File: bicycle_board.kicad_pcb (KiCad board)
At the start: 2 copper layers, 132 parts, among them J1 Conn_02x05_Odd_Even, J10 USB_A, J11 Conn_01x02, J12 Conn_01x04, J13 Conn_01x04, J2 USB_C_Receptacle_USB2.0_16P, J3 Conn_01x02, J4 Conn_01x02, J5 Micro_SD_Card, J6 Conn_01x08, J7 Conn_01x03, J8 Conn_01x02, J9 Conn_01x06, Q1 Q_NMOS_GSD, Q2 Q_NMOS_GSD, Q3 Q_NMOS_GSD, Q4 Q_NMOS_GSD, Q5 Q_NMOS_GSD, Q6 Si2302, Q7 Si2302, Q8 Q_PMOS_GSD, U1 TP4056, U10 MCP603-xCH, U11 BMP280, U12 MMC5633NJL, U13 NS4168, U14 ESP32-C3-WROOM-02U, U15 CH32V203C8T6, U16 PS7516, U17 TXB0108PW, U2 SGM2039, U3 IIM-42652, U4 QMI8610, U5 AHT20, U6 SGM2033-1.8, U7 74HC595, U8 74HC595, U9 PCA9306DC1, Y1 12MHz, Y2 32.768kHz

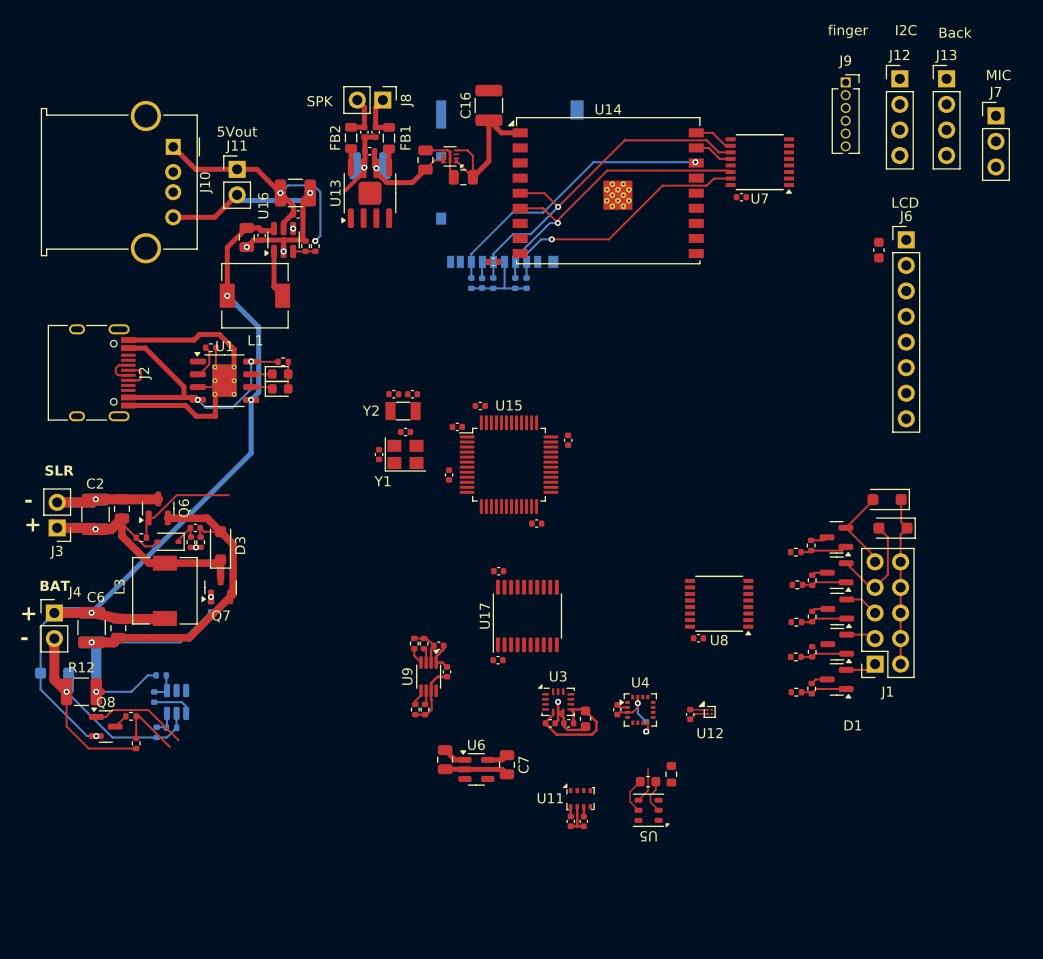
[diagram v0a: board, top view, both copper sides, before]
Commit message: 初步划定PCB边缘，改为紧凑布局
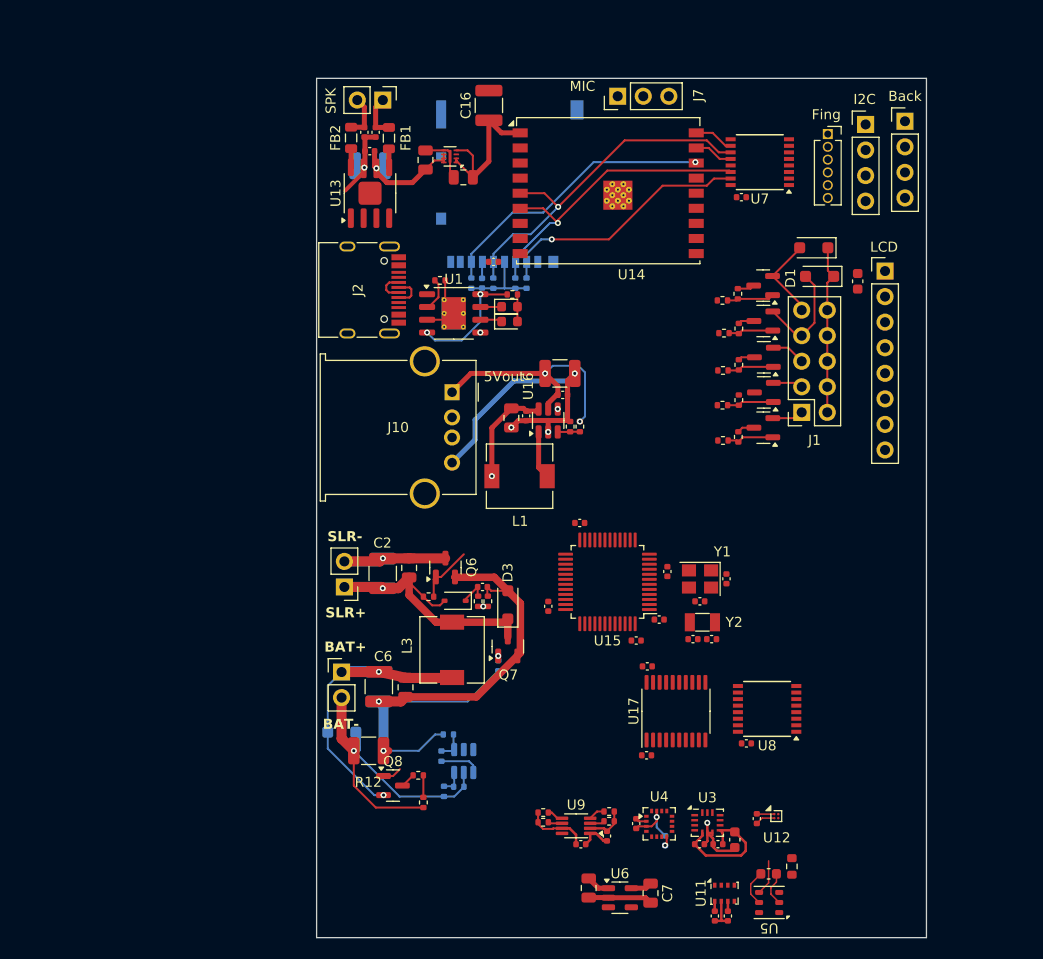
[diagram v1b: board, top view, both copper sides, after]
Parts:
- removed J11: Conn_01x02, Connector_PinHeader_2.54mm:PinHeader_1x02_P2.54mm_Vertical
- moved C23 39.9 mm to (139.8, 112.8), turned to 180 degrees
- moved J7 37.6 mm to (130.5, 58.9), turned to 90 degrees
- moved C22 37.0 mm to (138.0, 112.8), turned to 0 degrees
- moved J10 36.9 mm to (114.0, 88.3)
- moved C24 36.7 mm to (141.3, 106.8), turned to -90 degrees
- moved Y2 36.4 mm to (138.9, 111.2), turned to 180 degrees
- moved C25 33.7 mm to (138.7, 109.1), turned to 0 degrees
- moved C45 31.8 mm to (121.4, 90.6)
- moved C44 31.8 mm to (119.9, 90.8)
- moved C46 31.8 mm to (124.8, 86.4)
- moved C47 31.8 mm to (125.0, 88.6)
- moved L1 31.8 mm to (120.8, 96.6)
- moved R33 31.8 mm to (126.7, 91.7)
- moved R34 31.8 mm to (125.8, 91.7)
- moved U16 31.8 mm to (123.6, 91.1)
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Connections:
- net /power/5V_EN renamed /power/5VOUT_EN
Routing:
- net +BATT: track 94.8 -> 55.2 mm
- net GND: track 135.5 -> 113.1 mm
- net /power/VUSB: track 27.0 -> 11.8 mm
- net /batsamp_en: track 9.70 -> 1.92 mm
- net /PWM_solar: track 10.9 -> 5.76 mm
- net /ADC_Vbat: track 6.80 -> 2.18 mm
- net +5V: track 26.7 -> 24.2 mm
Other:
- board outline added: 60.6 x 85.4 mm
- board text added: "BAT+"
- board text added: "BAT-"
- board text added: "SLR+"
- board text added: "SLR-"
- board text removed: "+ -"
- board text removed: "- +"
- board text removed: "BAT"
- board text removed: "Back"
- board text removed: "I2C"
- board text removed: "LCD"
- board text removed: "SLR"
- board text removed: "SPK"
- board text removed: "finger"

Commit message: 收窄PCB宽度到47.4mm
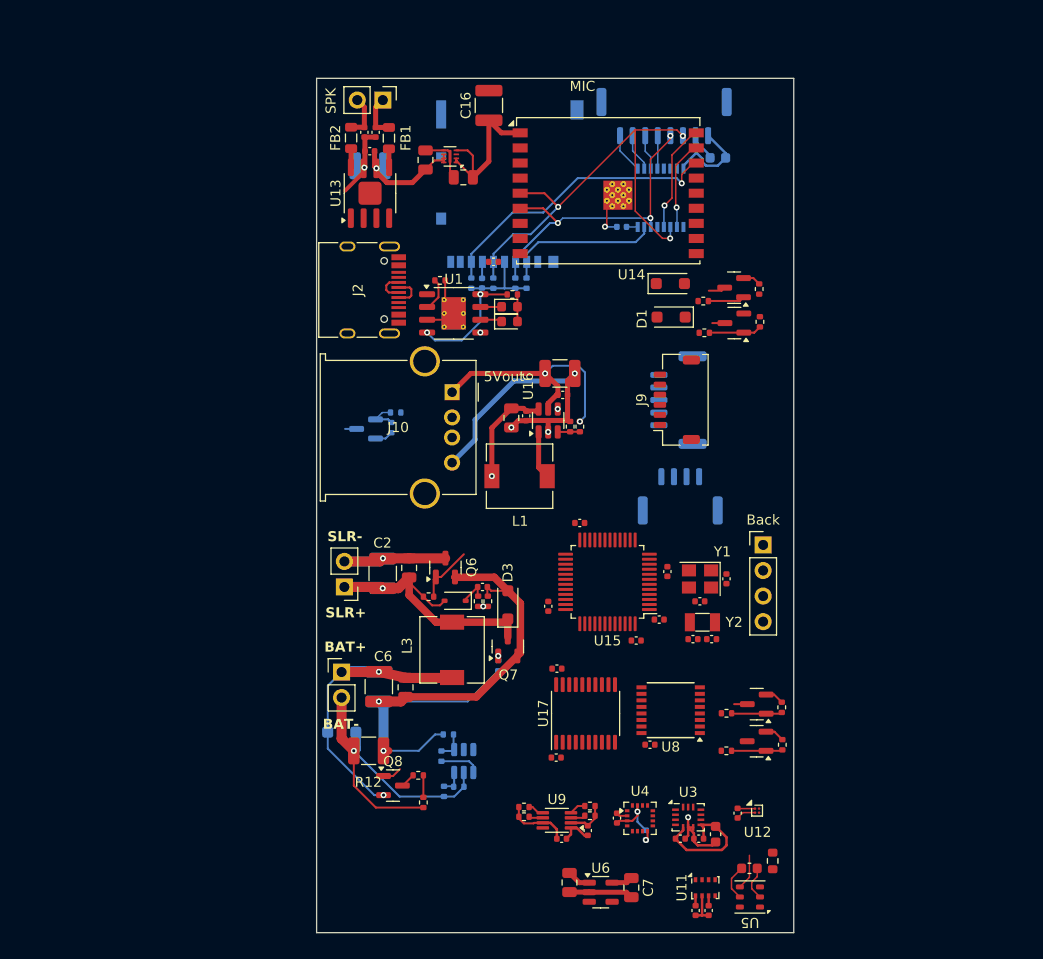
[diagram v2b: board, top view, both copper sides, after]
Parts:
- removed J1: Conn_02x05_Odd_Even, Connector_PinSocket_2.54mm:PinSocket_2x05_P2.54mm_Vertical
- C14, C42, Q1, R1, R2, U7: moved to B.Cu
- J12: footprint Connector_PinHeader_2.54mm:PinHeader_1x04_P2.54mm_Vertical -> Connector_JST:JST_GH_BM04B-GHS-TBT_1x04-1MP_P1.25mm_Vertical; moved to B.Cu
- J6: footprint Connector_PinHeader_2.54mm:PinHeader_1x08_P2.54mm_Vertical -> Connector_JST:JST_GH_BM08B-GHS-TBT_1x08-1MP_P1.25mm_Vertical; moved to B.Cu
- J7: value Conn_01x03 -> Conn_01x05; footprint Connector_PinHeader_2.54mm:PinHeader_1x03_P2.54mm_Vertical -> Connector_JST:JST_GH_BM05B-GHS-TBT_1x05-1MP_P1.25mm_Vertical; moved to B.Cu
- J9: footprint Connector_PinSocket_1.27mm:PinSocket_1x06_P1.27mm_Vertical -> Connector_JST:JST_SHL_SM06B-SHLS-TF_1x06-1MP_P1.00mm_Horizontal
- moved J13 44.4 mm to (145.0, 103.5)
- moved J12 41.3 mm to (136.7, 98.6)
- moved Q1 39.5 mm to (105.5, 91.9)
- moved Q2 34.7 mm to (144.3, 123.0)
- moved R3 34.5 mm to (146.9, 123.3)
- moved R1 34.5 mm to (108.0, 91.8), turned to -90 degrees
- moved Q3 34.5 mm to (144.3, 119.3)
- moved R7 34.3 mm to (141.3, 123.9)
- moved R4 34.3 mm to (146.8, 119.6)
- moved R8 34.1 mm to (141.3, 120.2)
- moved R2 32.6 mm to (108.4, 90.3), turned to 180 degrees
- moved J7 30.8 mm to (136.5, 89.1)
- moved J9 30.4 mm to (136.4, 89.0), turned to 90 degrees
- moved J6 26.8 mm to (135.1, 60.9), turned to 180 degrees
- moved C14 18.5 mm to (140.5, 65.0), turned to 0 degrees
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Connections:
- J7 pad 1: /I2SI_WS -> unconnected-(J7-Pin_1-Pad1)
- J7 pad 2: /I2SI_BCK -> unconnected-(J7-Pin_2-Pad2)
- J7 pad 3: /I2SI_SD -> /I2SI_WS
- Q1 pad 3: Net-(J1-Pin_1) -> unconnected-(Q1-D-Pad3)
- Q2 pad 3: Net-(J1-Pin_3) -> unconnected-(Q2-D-Pad3)
- Q3 pad 3: Net-(J1-Pin_5) -> Net-(D2-A)
- U14 pad 17: /595_RCLK -> /595_CLR
- U14 pad 18: /595_CLR -> /595_RCLK
- U7 pad 1: /SPI_CS_LCD -> /LCD_BL
- U7 pad 2: /SPI_CS_STM32 -> /SPI_CS_LCD
- U7 pad 3: /LED_WIFIBT -> /LCD_RST
- U7 pad 5: /LCD_RST -> unconnected-(U7-QF-Pad5)
- U7 pad 6: /LCD_BL -> /SPI_CS_STM32
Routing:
- net Net-(D1-K): track 16.9 -> 0.00 mm
- net GND: track 113.1 -> 125.9 mm, vias 7 -> 8
- net Net-(D1-A): track 12.3 -> 1.26 mm
- net /SPI_CS_SD: track 25.8 -> 15.6 mm, vias 1 -> 0
- net /SPI_SCLK: track 35.5 -> 44.7 mm, vias 1 -> 3
- net Net-(D2-A): track 10.2 -> 3.01 mm
- net /595_RCLK: track 3.87 -> 10.8 mm, vias 0 -> 1
- net /595_CLR: track 3.95 -> 8.93 mm, vias 0 -> 1
- net Net-(J1-Pin_1): track 4.83 -> 0.00 mm
- net /LCD_BL: track 0.00 -> 4.00 mm
- net +3.3V: track 32.5 -> 36.4 mm
- net /SPI_CS_LCD: track 0.00 -> 3.75 mm
- net /LCD_RST: track 0.00 -> 3.50 mm
- net Net-(J1-Pin_5): track 3.38 -> 0.00 mm
- net /LCD_DC: track 0.00 -> 3.29 mm
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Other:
- board size 60.6 x 85.4 mm -> 47.4 x 84.9 mm

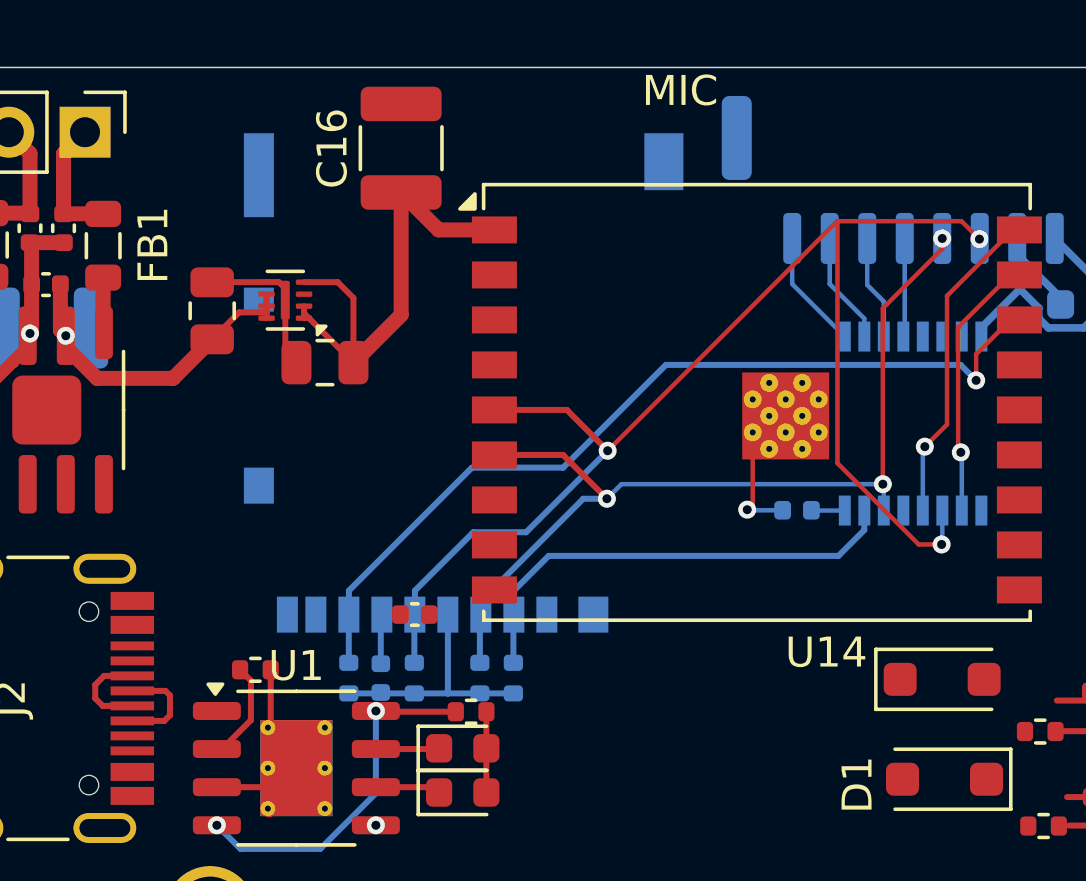
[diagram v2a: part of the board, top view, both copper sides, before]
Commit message: 画我现有的SD卡槽封装，应用到PCB
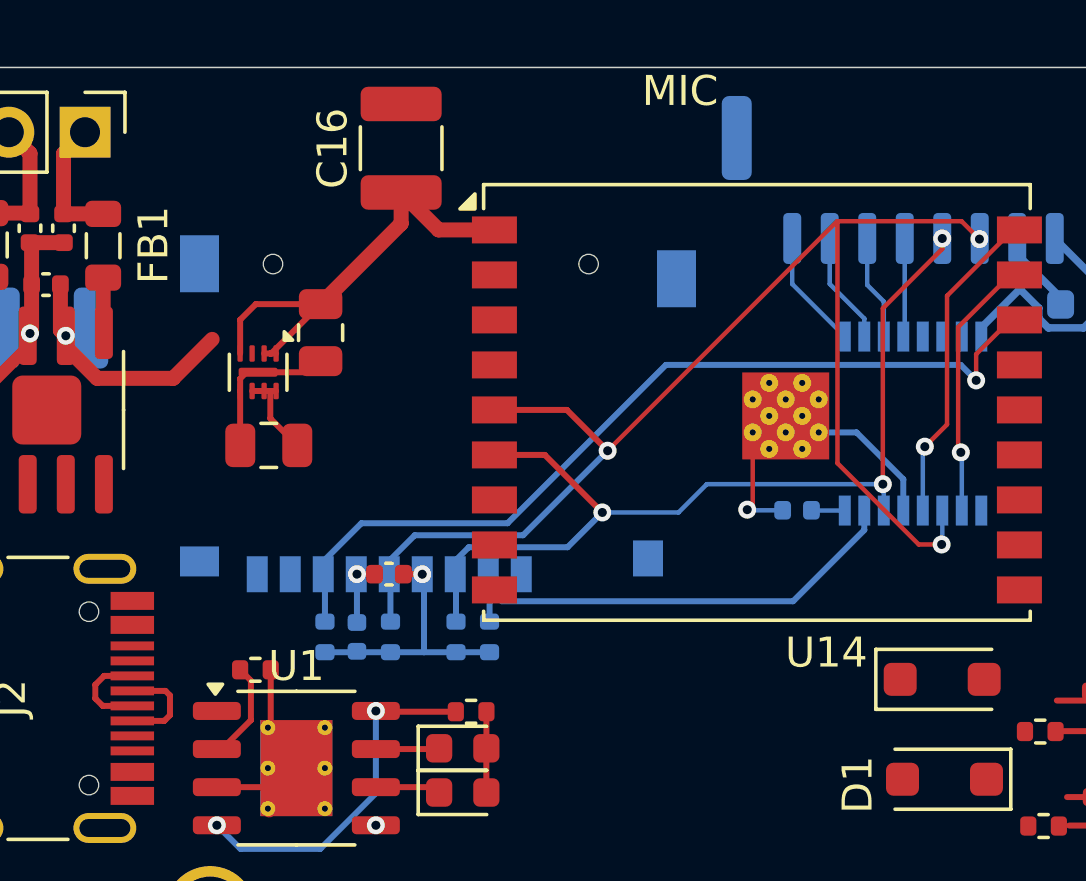
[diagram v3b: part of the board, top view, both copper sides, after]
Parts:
- removed J5: Micro_SD_Card, Connector_Card:microSD_HC_Hirose_DM3AT-SF-PEJM5
- added J1: Micro_SD_Card, Library:microSD_Slot_mybuy, B.Cu at (118.9, 66.3)
- moved C3 4.87 mm to (113.3, 69.7), turned to 180 degrees
- moved U2 2.57 mm to (112.9, 67.3), turned to -90 degrees
- moved C32 1.60 mm to (117.3, 74.0)
- moved C13 1.59 mm to (116.2, 76.1)
- moved R28 1.59 mm to (119.5, 76.1)
- moved R30 1.59 mm to (117.3, 76.1)
- moved R31 1.59 mm to (115.2, 76.1)
- moved R27 1.59 mm to (120.7, 76.1)
- moved C8 1.01 mm to (115.0, 65.9), turned to -90 degrees
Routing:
- net GND: track 125.9 -> 131.0 mm, vias 8 -> 9
- net +3.3V: track 36.4 -> 35.5 mm, vias 0 -> 1
- net /SPI_CS_SD: track 15.6 -> 16.4 mm

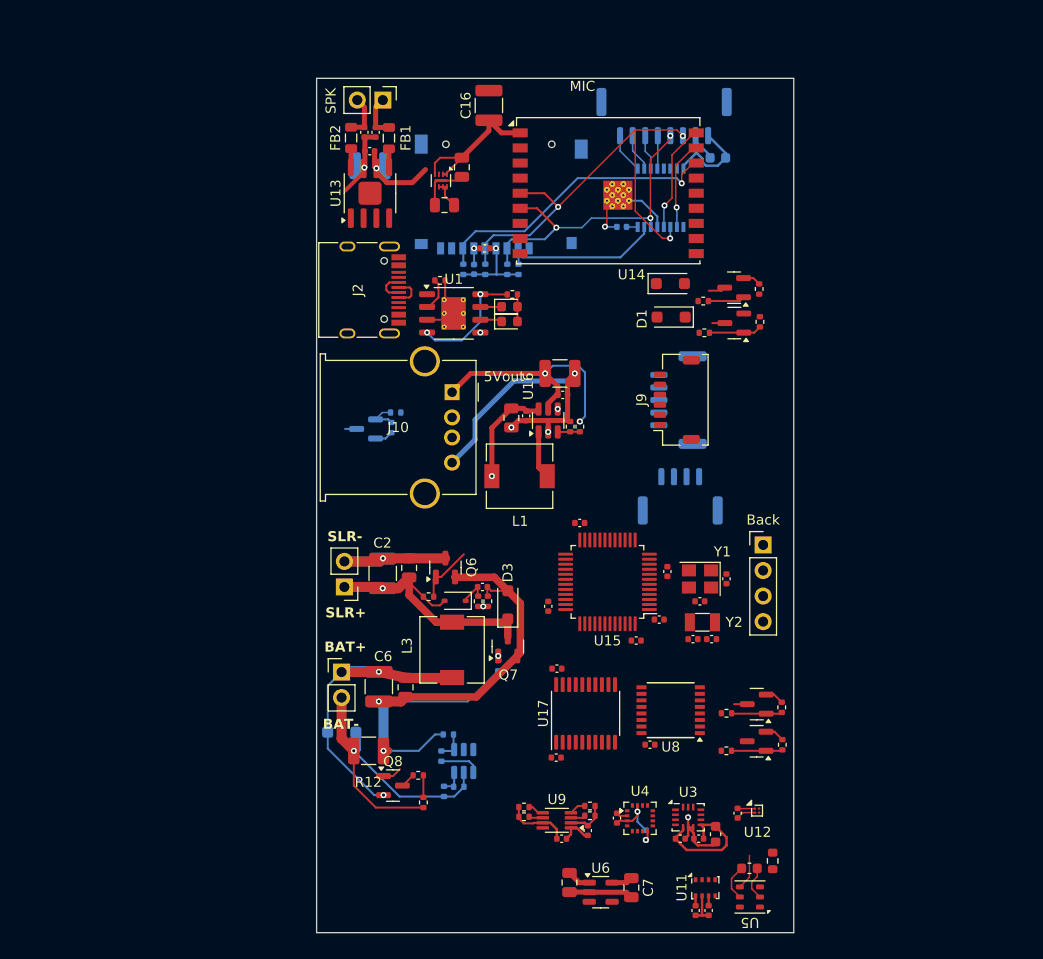
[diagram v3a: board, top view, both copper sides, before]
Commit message: PCB宽度进一步收缩到41.4mm，晶振改2016和2012，最小线距改0.15mm，添加一些布线
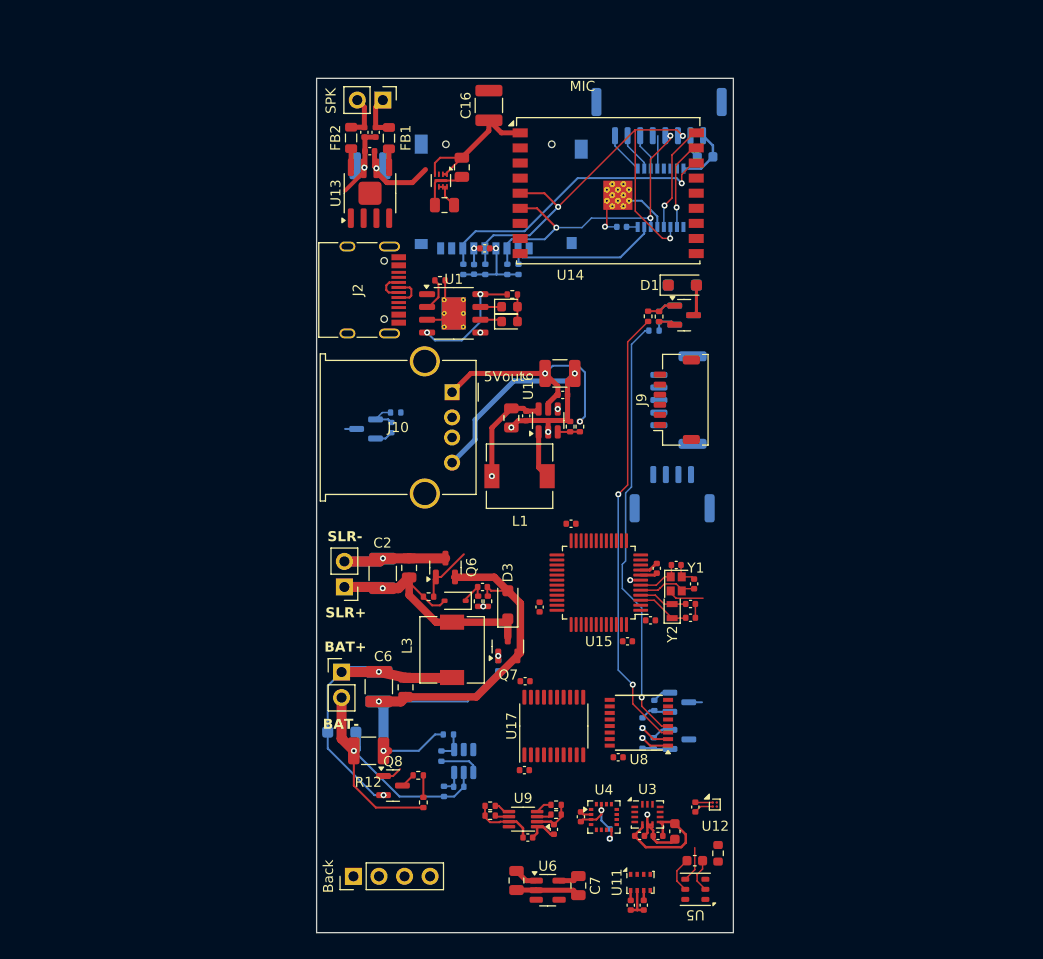
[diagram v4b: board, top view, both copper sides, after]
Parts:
- D2, Q2, Q3, Q5, R10, R3, R4, R6, R7, R8: moved to B.Cu
- Y1: footprint Crystal:Crystal_SMD_3225-4Pin_3.2x2.5mm -> Crystal:Crystal_SMD_2016-4Pin_2.0x1.6mm
- Y2: footprint Crystal:Crystal_SMD_3215-2Pin_3.2x1.5mm -> Crystal:Crystal_SMD_2012-2Pin_2.0x1.2mm
- moved J13 52.4 mm to (104.2, 136.4), turned to 90 degrees
- moved R3 12.8 mm to (134.1, 123.1)
- moved R4 12.7 mm to (134.1, 119.4)
- moved R6 10.3 mm to (134.6, 80.8)
- moved R5 10.0 mm to (134.6, 80.8), turned to -90 degrees
- moved R8 8.41 mm to (133.0, 121.2), turned to 90 degrees
- moved R7 8.37 mm to (133.0, 123.2), turned to -90 degrees
- moved Q3 7.70 mm to (136.6, 119.1), turned to 0 degrees
- moved Q2 7.67 mm to (136.6, 122.8), turned to 0 degrees
- moved C19 6.47 mm to (133.1, 139.3)
- moved C35 6.47 mm to (131.8, 139.3)
- moved U11 6.47 mm to (132.8, 137.0)
- moved R9 5.83 mm to (133.5, 80.7), turned to 90 degrees
- moved R10 5.71 mm to (134.1, 82.2)
- moved Q5 5.67 mm to (137.1, 80.6), turned to 0 degrees
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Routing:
- net /CH4: track 0.00 -> 44.5 mm, vias 0 -> 2
- net /CH5: track 0.00 -> 42.9 mm, vias 0 -> 1
- net GND: track 131.0 -> 137.2 mm
- net Net-(U15-PD0): track 0.00 -> 6.09 mm
- net Net-(U15-PC14): track 0.00 -> 5.23 mm
- net Net-(U15-PC15): track 0.00 -> 4.83 mm
- net Net-(U15-PD1): track 0.00 -> 4.53 mm
- net /CH3: track 0.00 -> 3.00 mm, vias 0 -> 1
- net /CH2: track 0.00 -> 2.86 mm, vias 0 -> 1
- net Net-(Q4-G): track 4.90 -> 2.89 mm
- net Net-(Q2-G): track 4.76 -> 2.78 mm
- net Net-(D1-A): track 1.26 -> 3.10 mm
- net Net-(Q4-S): track 0.00 -> 1.68 mm
- net Net-(Q3-G): track 4.72 -> 3.07 mm
- net +3.3V: track 35.5 -> 37.0 mm
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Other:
- board size 47.4 x 84.9 mm -> 41.4 x 84.9 mm

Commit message: 添加CERN-OHL-S许可证、README.md文件
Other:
- board text added: "Copyright (C) 2024 Xu Ruijun License under CERN-OHL-S v2"
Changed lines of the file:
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@@
 		(tags "resistor")
 		(property "Reference" "R10"
-			(at 0 1.17 360)
+			(at 0 1.17 0)
 			(layer "B.SilkS")
 			(hide yes)
@@
 		)
 		(property "Value" "470"
-			(at 0 -1.17 360)
+			(at 0 -1.17 0)
 			(layer "B.Fab")
 			(effects
@@
 		)
 		(fp_text user "${REFERENCE}"
-			(at 0 0 360)
+			(at 0 0 0)
 			(layer "B.Fab")
 			(effects
@@
 		(layer "Edge.Cuts")
 	)
+	(gr_text "Copyright (C) 2024  Xu Ruijun\nLicense under CERN-OHL-S v2"
+		(at 126.365 133.223 0)
+		(layer "B.SilkS")
+		(effects
+			(font
+				(size 1 1)
+				(thickness 0.1)
+			)
+			(justify left bottom mirror)
+		)
+	)
 	(gr_text "BAT-"
